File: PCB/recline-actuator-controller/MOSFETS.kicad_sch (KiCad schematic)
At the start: 0 parts

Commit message: Recline Actuator Control
Recline controller board schematic and Recline actuator board schematics. Actuator control board schematic 90% complete.
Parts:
- added D10, D12, D3, D6, D8: LTST-C194TBKT, AVR-KiCAD-Lib-Diodes:LED0603, symbol AVR-KiCAD-Lib-Diodes:LTST-C194TBKT
- added D11, D4, D5, D7, D9: B240A-13-F, AVR-KiCAD-Lib-Diodes:B240A-13-F, symbol AVR-KiCAD-Lib-Diodes:B240A-13-F
- added J10, J11, J7, J8, J9: 1757242, AVR-KiCAD-Lib-Connectors:PhoenixContact_MSTBA-G_02x5.08mm_Angled, symbol AVR-KiCAD-Lib-Connectors:1757242
- added Q1, Q2, Q3, Q4, Q5: PSMN7R0-60YS,115, AVR-KiCAD-Lib-Transistors:IC5_PSMN7R0-60YS_115_NEX-L, symbol AVR-KiCAD-Lib-Transistors:PSMN7R0-60YS,115
- added R13, R17, R20, R23, R26: RC0805FR-07100KL, AVR-KiCAD-Lib-Resistors:R0805, symbol AVR-KiCAD-Lib-Resistors:RC0805FR-07100KL
- added R14, R18, R21, R24, R27: RC0805FR-071K96L, AVR-KiCAD-Lib-Resistors:R0805, symbol AVR-KiCAD-Lib-Resistors:RC0805FR-071K96L
- added R15, R16, R19, R22, R25: RC0805FR-0710RL, AVR-KiCAD-Lib-Resistors:R0805, symbol AVR-KiCAD-Lib-Resistors:RC0805FR-0710RL
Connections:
- new net: D7.1, D8.2, J8.2, Q3.5 (D)
- new net: D3.2, D4.1, J11.2, Q1.5 (D)
- new net: Q4.4 (G), R22.2
- new net: D10.2, D9.1, J9.2, Q4.5 (D)
- new net: Q5.4 (G), R25.2
- new net: D11.1, D12.2, J10.2, Q5.5 (D)
- new net: D5.1, D6.2, J7.2, Q2.5 (D)
- new net: D6.1, R18.1
- new net: D3.1, R14.1
- new net: Q1.4 (G), R15.2
- new net: Q3.4 (G), R19.2
- new net: Q2.4 (G), R16.2
- new net: D12.1, R27.1
- new net: D10.1, R24.1
- new net: D8.1, R21.1
- new net +24V: D11.2, D4.2, D5.2, D7.2, D9.2, J10.1, J11.1, J7.1, J8.1, J9.1, R14.2, R18.2, R21.2, R24.2, R27.2
- new net AIR_COMP: R25.1, R26.1
- new net GND: Q1.1, Q1.2 (S), Q1.3, Q2.1, Q2.2 (S), Q2.3, Q3.1, Q3.2 (S), Q3.3, Q4.1, Q4.2 (S), Q4.3, Q5.1, Q5.2 (S), Q5.3, R13.2, R17.2, R20.2, R23.2, R26.2
- new net SOLENOID_0: R13.1, R15.1
- new net SOLENOID_1: R16.1, R17.1
- new net SOLENOID_2: R19.1, R20.1
- new net SOLENOID_3: R22.1, R23.1
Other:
- note added: "Solenoid and Air Compressor MOSFETS"

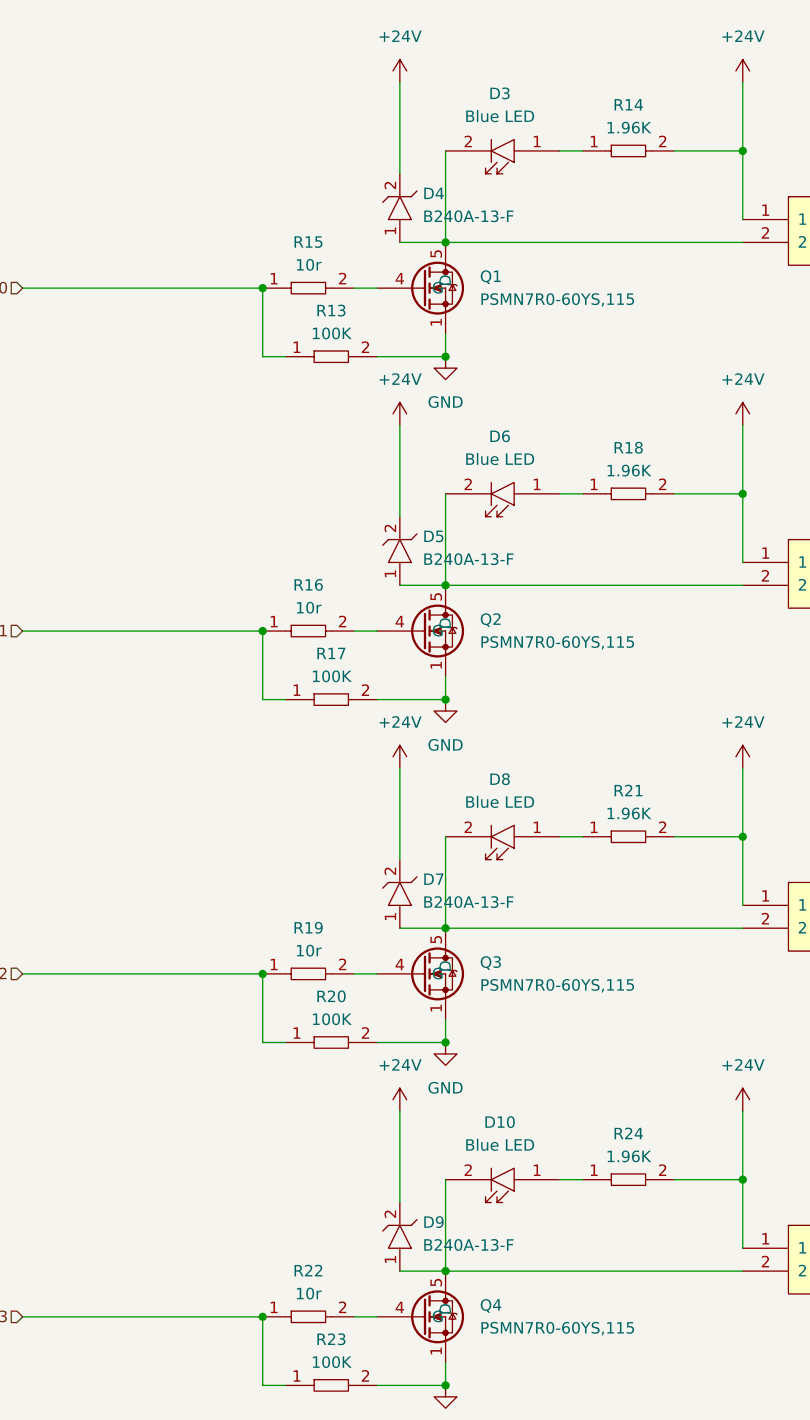
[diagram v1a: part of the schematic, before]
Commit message: Actuator Control Board  MOSFET
Swapped Actuator control board MOSFET over to a more thermally efficient part
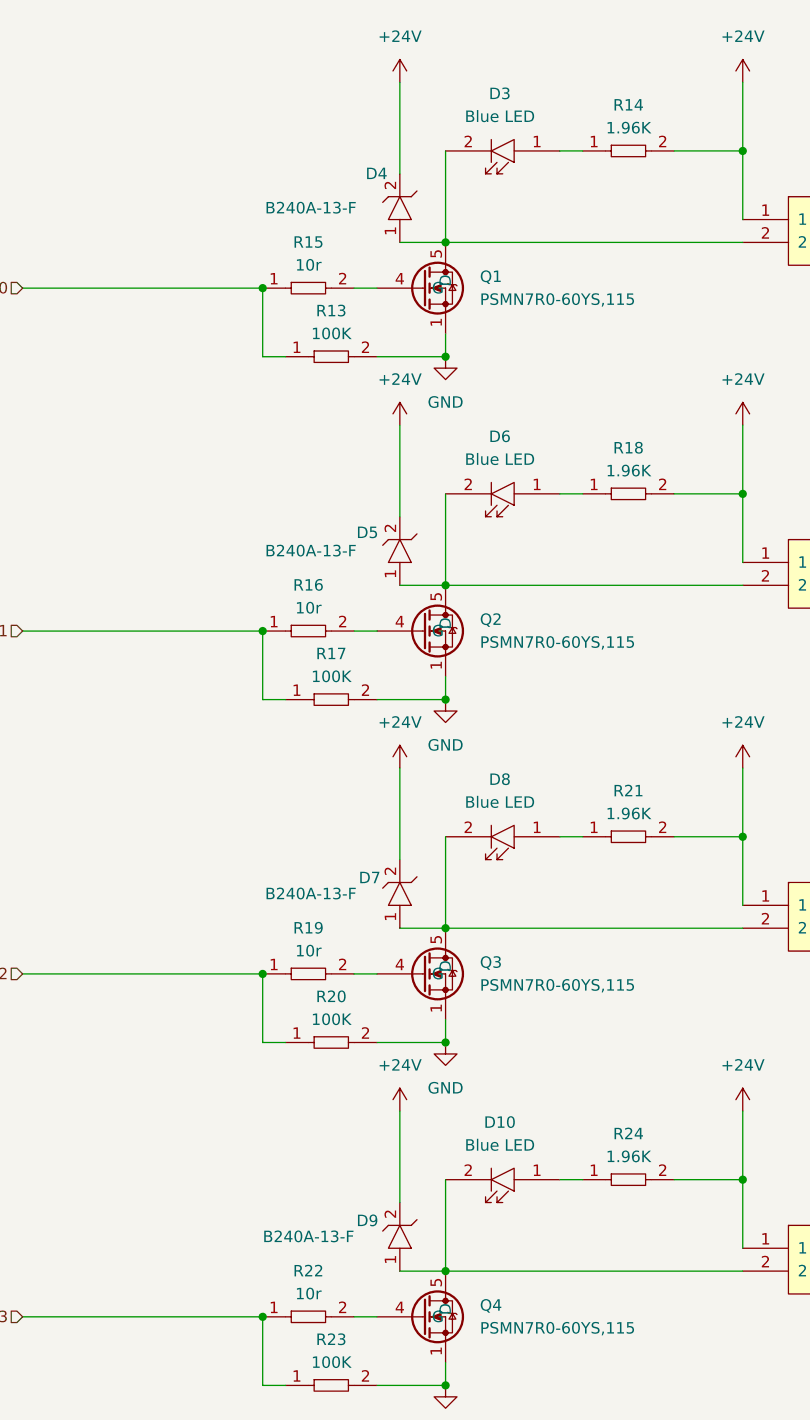
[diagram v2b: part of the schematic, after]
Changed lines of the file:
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@@
 		(on_board yes)
 		(dnp no)
-		(fields_autoplaced yes)
 		(property "Reference" "D5"
-			(at 91.44 83.5024 90)
+			(at 84.074 83.058 90)
 			(effects
 				(font
@@
 		)
 		(property "_Value_" "B240A-13-F"
-			(at 91.44 86.0424 90)
+			(at 73.914 85.09 90)
 			(effects
 				(font
@@
 		(on_board yes)
 		(dnp no)
-		(fields_autoplaced yes)
 		(property "Reference" "D7"
-			(at 91.44 121.6024 90)
+			(at 84.328 121.412 90)
 			(effects
 				(font
@@
 		)
 		(property "_Value_" "B240A-13-F"
-			(at 91.44 124.1424 90)
+			(at 73.914 123.19 90)
 			(effects
 				(font
@@
 		(on_board yes)
 		(dnp no)
-		(fields_autoplaced yes)
 		(property "Reference" "D4"
-			(at 91.44 45.4024 90)
+			(at 85.09 43.18 90)
 			(effects
 				(font
@@
 		)
 		(property "_Value_" "B240A-13-F"
-			(at 91.44 47.9424 90)
+			(at 73.914 46.99 90)
 			(effects
 				(font
@@
 		(on_board yes)
 		(dnp no)
-		(fields_autoplaced yes)
 		(property "Reference" "D9"
-			(at 91.44 159.7024 90)
+			(at 84.074 159.512 90)
 			(effects
 				(font
@@
 		)
 		(property "_Value_" "B240A-13-F"
-			(at 91.44 162.2424 90)
+			(at 73.66 161.29 90)
 			(effects
 				(font
